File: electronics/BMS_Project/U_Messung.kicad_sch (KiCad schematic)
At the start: 22 parts, among them J1 Conn_01x01_Socket, J2 Conn_01x01_Socket, J3 Conn_01x01_Socket, J4 Conn_01x01_Socket, U1 LM358, U2 LM358

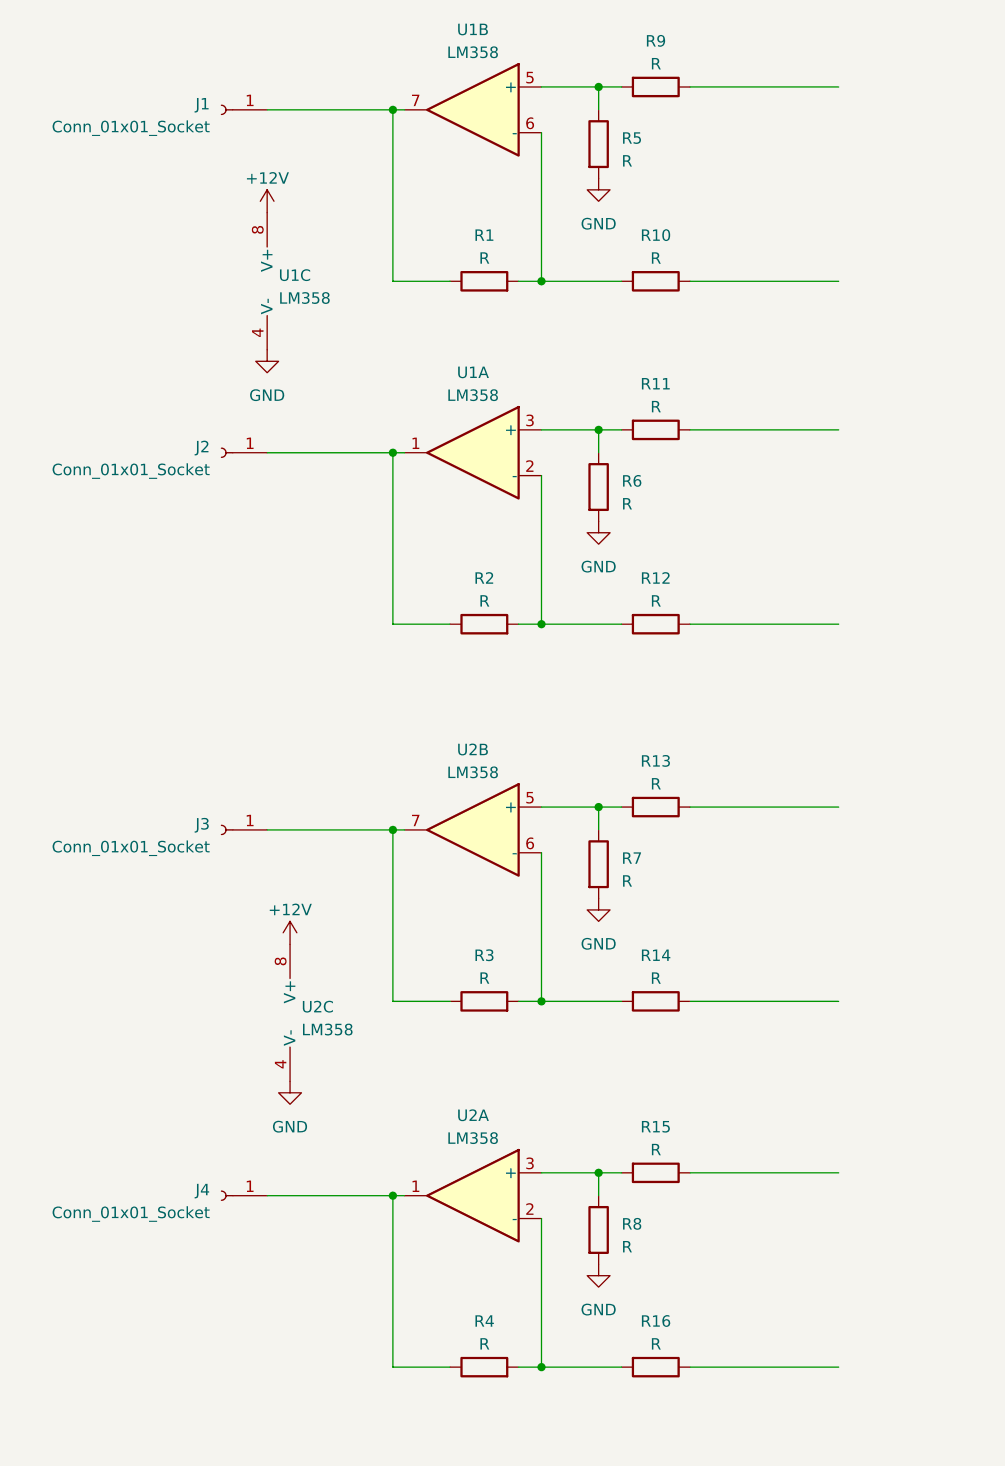
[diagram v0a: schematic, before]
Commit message: Started working on schematic segmentation and added first labels
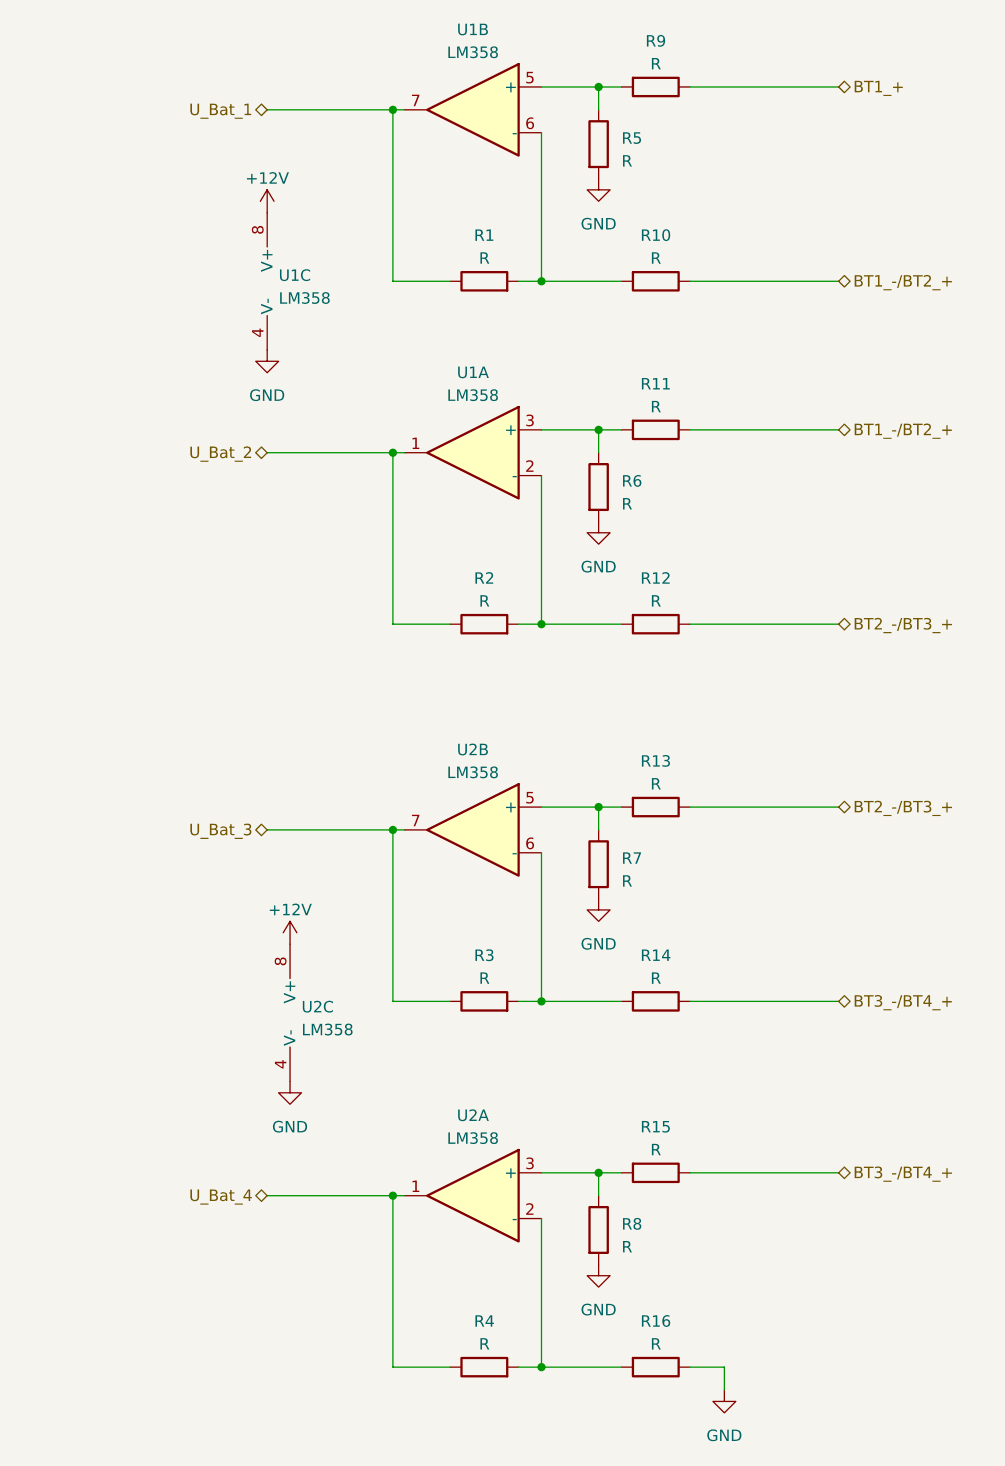
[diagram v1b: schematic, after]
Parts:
- removed J1, J2, J3, J4: Conn_01x01_Socket, symbol Connector:Conn_01x01_Socket
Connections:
- net GND: now also R16.1
- net U_Bat_1: now reaches R1.1, U1.7
- net U_Bat_4: now reaches R4.1, U2.1
- net U_Bat_3: now reaches R3.1, U2.7
- net BT1_+: now reaches R9.1
- net U_Bat_2: now reaches R2.1, U1.1
- net BT3_-/BT4_+: now reaches R15.1
- net BT3_-/BT4_+: now also R14.1
- net BT1_-/BT2_+: now reaches R11.1
- net BT1_-/BT2_+: now also R10.1
- net BT2_-/BT3_+: now reaches R12.1
- net BT2_-/BT3_+: now also R13.1
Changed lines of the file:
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@@
+    (stroke (width 0) (type default))
+  )
+  (wire (pts (xy 110.49 170.18) (xy 114.3 170.18))
     (stroke (width 0) (type default))
   )
@@
     (stroke (width 0) (type default))
   )
+  (wire (pts (xy 114.3 172.72) (xy 114.3 170.18))
+    (stroke (width 0) (type default))
+  )
   (wire (pts (xy 110.49 27.94) (xy 127 27.94))
     (stroke (width 0) (type default))
@@
     (stroke (width 0) (type default))
   )
-  (wire (pts (xy 110.49 170.18) (xy 127 170.18))
-    (stroke (width 0) (type default))
-  )
   (wire (pts (xy 77.47 30.48) (xy 78.74 30.48))
     (stroke (width 0) (type default))
@@
     (stroke (width 0) (type default))
   )
-  (symbol (lib_id "Connector:Conn_01x01_Socket") (at 58.42 30.48 0) (mirror y) (unit 1)
-    (in_bom yes) (on_board yes) (dnp no)
-    (property "Reference" "J1" (at 57.15 29.845 0)
-      (effects (font (size 1.27 1.27)) (justify left))
-    )
-    (property "Value" "Conn_01x01_Socket" (at 57.15 32.385 0)
-      (effects (font (size 1.27 1.27)) (justify left))
-    )
-    (property "Footprint" "" (at 58.42 30.48 0)
-      (effects (font (size 1.27 1.27)) hide)
-    )
-    (property "Datasheet" "~" (at 58.42 30.48 0)
-      (effects (font (size 1.27 1.27)) hide)
-    )
-    (pin "1")
-    (instances
-      (project "BMS_Project"
-        (path "/524e7f14-feb0-4ca2-9425-a347c869bfa6/d8f12774-e346-4091-abf5-b4c43e81469c"
-          (reference "J1") (unit 1)
-        )
-      )
-      (project "Test_Projekt"
-        (path "/d5b120ca-a0f0-4b3f-8fab-ca010d94ac2e"
-          (reference "J4") (unit 1)
-        )
-      )
-    )
+  (hierarchical_label "BT1_+" (shape bidirectional) (at 127 27.94 0) (fields_autoplaced)
+    (effects (font (size 1.27 1.27)) (justify left))
+  )
+  (hierarchical_label "U_Bat_3" (shape bidirectional) (at 63.5 110.49 180) (fields_autoplaced)
+    (effects (font (size 1.27 1.27)) (justify right))
+  )
+  (hierarchical_label "U_Bat_4" (shape bidirectional) (at 63.5 151.13 180) (fields_autoplaced)
+    (effects (font (size 1.27 1.27)) (justify right))
+  )
+  (hierarchical_label "BT1_-{slash}BT2_+" (shape bidirectional) (at 127 49.53 0) (fields_autoplaced)
+    (effects (font (size 1.27 1.27)) (justify left))
+  )
+  (hierarchical_label "U_Bat_1" (shape bidirectional) (at 63.5 30.48 180) (fields_autoplaced)
+    (effects (font (size 1.27 1.27)) (justify right))
+  )
+  (hierarchical_label "BT1_-{slash}BT2_+" (shape bidirectional) (at 127 66.04 0) (fields_autoplaced)
+    (effects (font (size 1.27 1.27)) (justify left))
+  )
+  (hierarchical_label "U_Bat_2" (shape bidirectional) (at 63.5 68.58 180) (fields_autoplaced)
+    (effects (font (size 1.27 1.27)) (justify right))
+  )
+  (hierarchical_label "BT3_-{slash}BT4_+" (shape bidirectional) (at 127 148.59 0) (fields_autoplaced)
+    (effects (font (size 1.27 1.27)) (justify left))
+  )
+  (hierarchical_label "BT2_-{slash}BT3_+" (shape bidirectional) (at 127 107.95 0) (fields_autoplaced)
+    (effects (font (size 1.27 1.27)) (justify left))
+  )
+  (hierarchical_label "BT2_-{slash}BT3_+" (shape bidirectional) (at 127 87.63 0) (fields_autoplaced)
+    (effects (font (size 1.27 1.27)) (justify left))
+  )
+  (hierarchical_label "BT3_-{slash}BT4_+" (shape bidirectional) (at 127 129.54 0) (fields_autoplaced)
+    (effects (font (size 1.27 1.27)) (justify left))
   )
   (symbol (lib_id "Device:R") (at 100.33 114.3 0) (unit 1)
@@
     )
   )
-  (symbol (lib_id "Connector:Conn_01x01_Socket") (at 58.42 68.58 0) (mirror y) (unit 1)
-    (in_bom yes) (on_board yes) (dnp no)
-    (property "Reference" "J2" (at 57.15 67.945 0)
-      (effects (font (size 1.27 1.27)) (justify left))
-    )
-    (property "Value" "Conn_01x01_Socket" (at 57.15 70.485 0)
-      (effects (font (size 1.27 1.27)) (justify left))
-    )
-    (property "Footprint" "" (at 58.42 68.58 0)
-      (effects (font (size 1.27 1.27)) hide)
-    )
-    (property "Datasheet" "~" (at 58.42 68.58 0)
-      (effects (font (size 1.27 1.27)) hide)
-    )
-    (pin "1")
-    (instances
-      (project "BMS_Project"
-        (path "/524e7f14-feb0-4ca2-9425-a347c869bfa6/d8f12774-e346-4091-abf5-b4c43e81469c"
-          (reference "J2") (unit 1)
-        )
-      )
-      (project "Test_Projekt"
-        (path "/d5b120ca-a0f0-4b3f-8fab-ca010d94ac2e"
-          (reference "J3") (unit 1)
-        )
-      )
-    )
-  )
   (symbol (lib_id "power:GND") (at 66.04 138.43 0) (unit 1)
     (in_bom yes) (on_board yes) (dnp no) (fields_autoplaced)
@@
         (path "/d5b120ca-a0f0-4b3f-8fab-ca010d94ac2e"
           (reference "R7") (unit 1)
-        )
-      )
-    )
-  )
-  (symbol (lib_id "Connector:Conn_01x01_Socket") (at 58.42 151.13 0) (mirror y) (unit 1)
-    (in_bom yes) (on_board yes) (dnp no)
-    (property "Reference" "J4" (at 57.15 150.495 0)
-      (effects (font (size 1.27 1.27)) (justify left))
-    )
-    (property "Value" "Conn_01x01_Socket" (at 57.15 153.035 0)
-      (effects (font (size 1.27 1.27)) (justify left))
-    )
-    (property "Footprint" "" (at 58.42 151.13 0)
-      (effects (font (size 1.27 1.27)) hide)
-    )
-    (property "Datasheet" "~" (at 58.42 151.13 0)
-      (effects (font (size 1.27 1.27)) hide)
-    )
-    (pin "1")
-    (instances
-      (project "BMS_Project"
-        (path "/524e7f14-feb0-4ca2-9425-a347c869bfa6/d8f12774-e346-4091-abf5-b4c43e81469c"
-          (reference "J4") (unit 1)
-        )
-      )
-      (project "Test_Projekt"
-        (path "/d5b120ca-a0f0-4b3f-8fab-ca010d94ac2e"
-          (reference "J1") (unit 1)
         )
       )
@@
     )
   )
-  (symbol (lib_id "Connector:Conn_01x01_Socket") (at 58.42 110.49 0) (mirror y) (unit 1)
-    (in_bom yes) (on_board yes) (dnp no)
-    (property "Reference" "J3" (at 57.15 109.855 0)
-      (effects (font (size 1.27 1.27)) (justify left))
-    )
-    (property "Value" "Conn_01x01_Socket" (at 57.15 112.395 0)
-      (effects (font (size 1.27 1.27)) (justify left))
-    )
-    (property "Footprint" "" (at 58.42 110.49 0)
-      (effects (font (size 1.27 1.27)) hide)
-    )
-    (property "Datasheet" "~" (at 58.42 110.49 0)
-      (effects (font (size 1.27 1.27)) hide)
-    )
-    (pin "1")
-    (instances
-      (project "BMS_Project"
-        (path "/524e7f14-feb0-4ca2-9425-a347c869bfa6/d8f12774-e346-4091-abf5-b4c43e81469c"
-          (reference "J3") (unit 1)
-        )
-      )
-      (project "Test_Projekt"
-        (path "/d5b120ca-a0f0-4b3f-8fab-ca010d94ac2e"
-          (reference "J2") (unit 1)
-        )
-      )
-    )
-  )
   (symbol (lib_id "Device:R") (at 106.68 87.63 270) (unit 1)
     (in_bom yes) (on_board yes) (dnp no) (fields_autoplaced)
@@
         )
       )
+    )
+  )
+  (symbol (lib_id "power:GND") (at 114.3 172.72 0) (unit 1)
+    (in_bom yes) (on_board yes) (dnp no) (fields_autoplaced)
+    (property "Reference" "#PWR026" (at 114.3 179.07 0)
+      (effects (font (size 1.27 1.27)) hide)
+    )
+    (property "Value" "GND" (at 114.3 177.8 0)
+      (effects (font (size 1.27 1.27)))
+    )
+    (property "Footprint" "" (at 114.3 172.72 0)
+      (effects (font (size 1.27 1.27)) hide)
+    )
+    (property "Datasheet" "" (at 114.3 172.72 0)
+      (effects (font (size 1.27 1.27)) hide)
+    )
+    (pin "1")
+    (instances
+      (project "BMS_Project"
+        (path "/524e7f14-feb0-4ca2-9425-a347c869bfa6/d8f12774-e346-4091-abf5-b4c43e81469c"
+          (reference "#PWR026") (unit 1)
+        )
+      )
+      (project "Test_Projekt"
+        (path "/d5b120ca-a0f0-4b3f-8fab-ca010d94ac2e"
+          (reference "#PWR025") (unit 1)
+        )
+      )

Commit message: added values to the parts
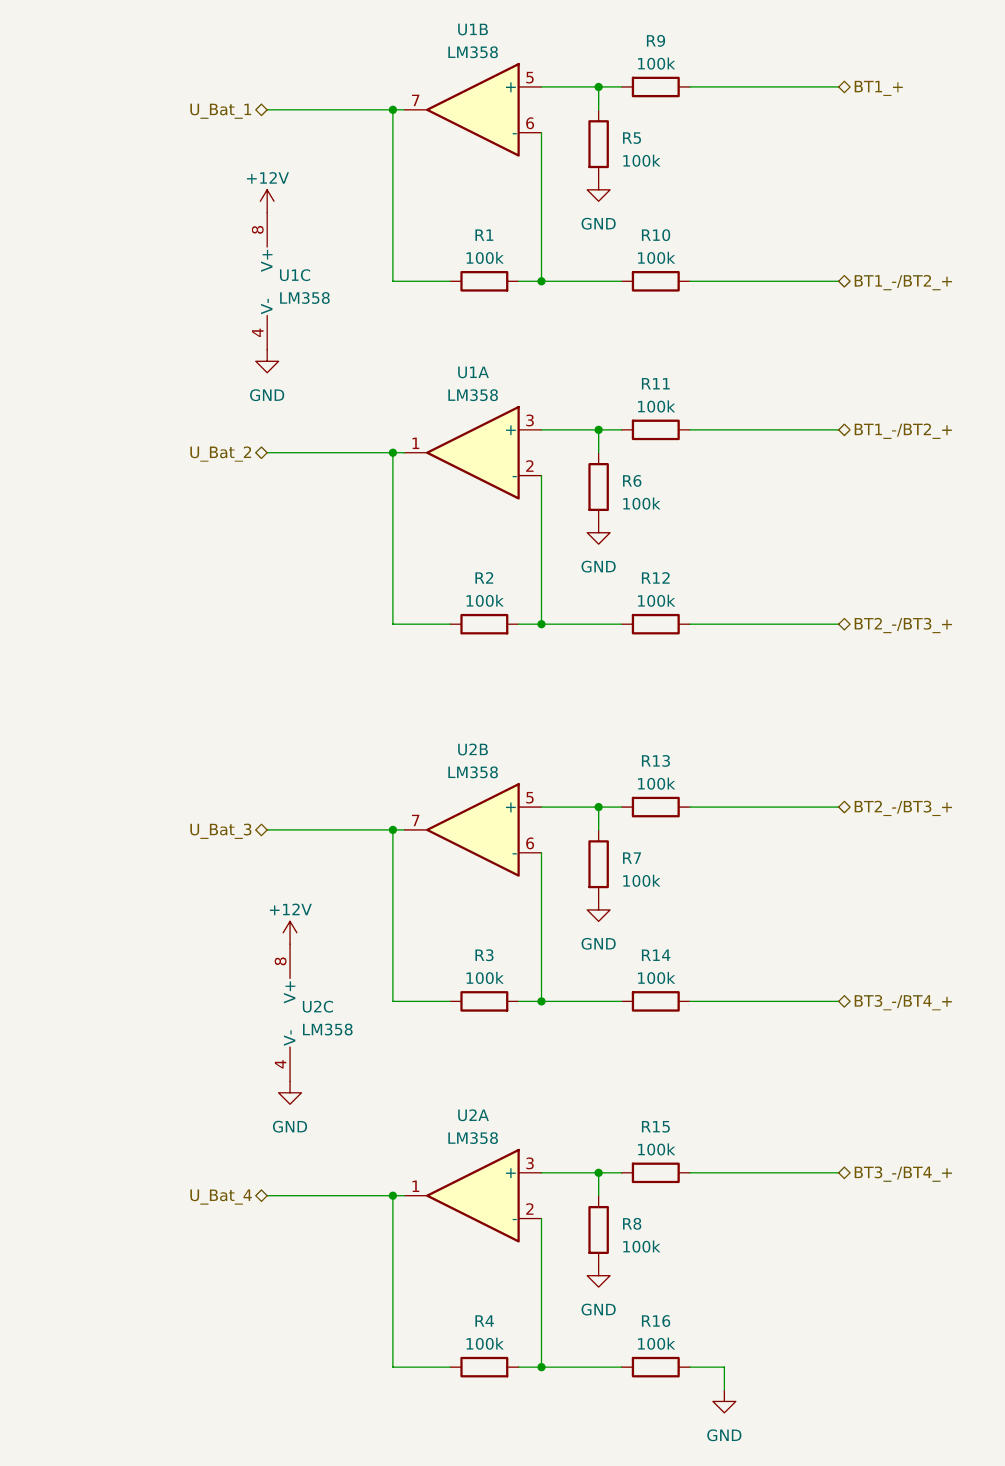
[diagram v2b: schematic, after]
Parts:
- R1, R10, R11, R12, R13, R14, R15, R16, R2, R3, R4, R5, R6, R7, R8, R9: value R -> 100k
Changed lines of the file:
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@@
       (effects (font (size 1.27 1.27)) (justify left))
     )
-    (property "Value" "R" (at 102.87 116.205 0)
+    (property "Value" "100k" (at 102.87 116.205 0)
       (effects (font (size 1.27 1.27)) (justify left))
     )
@@
       (effects (font (size 1.27 1.27)))
     )
-    (property "Value" "R" (at 87.63 167.64 90)
+    (property "Value" "100k" (at 87.63 167.64 90)
       (effects (font (size 1.27 1.27)))
     )
@@
       (effects (font (size 1.27 1.27)))
     )
-    (property "Value" "R" (at 106.68 25.4 90)
+    (property "Value" "100k" (at 106.68 25.4 90)
       (effects (font (size 1.27 1.27)))
     )
@@
       (effects (font (size 1.27 1.27)) (justify left))
     )
-    (property "Value" "R" (at 102.87 156.845 0)
+    (property "Value" "100k" (at 102.87 156.845 0)
       (effects (font (size 1.27 1.27)) (justify left))
     )
@@
       (effects (font (size 1.27 1.27)))
     )
-    (property "Value" "R" (at 87.63 127 90)
+    (property "Value" "100k" (at 87.63 127 90)
       (effects (font (size 1.27 1.27)))
     )
@@
       (effects (font (size 1.27 1.27)))
     )
-    (property "Value" "R" (at 106.68 146.05 90)
+    (property "Value" "100k" (at 106.68 146.05 90)
       (effects (font (size 1.27 1.27)))
     )
@@
       (effects (font (size 1.27 1.27)))
     )
-    (property "Value" "R" (at 106.68 127 90)
+    (property "Value" "100k" (at 106.68 127 90)
       (effects (font (size 1.27 1.27)))
     )
@@
       (effects (font (size 1.27 1.27)))
     )
-    (property "Value" "R" (at 106.68 63.5 90)
+    (property "Value" "100k" (at 106.68 63.5 90)
       (effects (font (size 1.27 1.27)))
     )
@@
       (effects (font (size 1.27 1.27)) (justify left))
     )
-    (property "Value" "R" (at 102.87 74.295 0)
+    (property "Value" "100k" (at 102.87 74.295 0)
       (effects (font (size 1.27 1.27)) (justify left))
     )
@@
       (effects (font (size 1.27 1.27)))
     )
-    (property "Value" "R" (at 106.68 85.09 90)
+    (property "Value" "100k" (at 106.68 85.09 90)
       (effects (font (size 1.27 1.27)))
     )
@@
       (effects (font (size 1.27 1.27)))
     )
-    (property "Value" "R" (at 87.63 46.99 90)
+    (property "Value" "100k" (at 87.63 46.99 90)
       (effects (font (size 1.27 1.27)))
     )
@@
       (effects (font (size 1.27 1.27)))
     )
-    (property "Value" "R" (at 87.63 85.09 90)
+    (property "Value" "100k" (at 87.63 85.09 90)
       (effects (font (size 1.27 1.27)))
     )
@@
       (effects (font (size 1.27 1.27)))
     )
-    (property "Value" "R" (at 106.68 167.64 90)
+    (property "Value" "100k" (at 106.68 167.64 90)
       (effects (font (size 1.27 1.27)))
     )
@@
       (effects (font (size 1.27 1.27)) (justify left))
     )
-    (property "Value" "R" (at 102.87 36.195 0)
+    (property "Value" "100k" (at 102.87 36.195 0)
       (effects (font (size 1.27 1.27)) (justify left))
     )
@@
       (effects (font (size 1.27 1.27)))
     )
-    (property "Value" "R" (at 106.68 46.99 90)
+    (property "Value" "100k" (at 106.68 46.99 90)
       (effects (font (size 1.27 1.27)))
     )
@@
       (effects (font (size 1.27 1.27)))
     )
-    (property "Value" "R" (at 106.68 105.41 90)
-      (effects (font (size 1.27 1.27)))
-    )
+    (property "Value" "100k" (at 106.68 105.41 90)
+      (effects (font (size 1.27 1.27)))
+    )
